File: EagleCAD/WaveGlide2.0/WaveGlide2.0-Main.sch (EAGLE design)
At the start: 58 parts, among them CN3 0, IC1 MC33502D, K2 MS-20-310-HN, Q2 reset, U1 ATMEGA328P_TQFP, U2 BMP180, U3 MPXV7002, U4 TPS55340PWP, U5 UG-2828GDEDF11, U6 TPS61222DCKR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

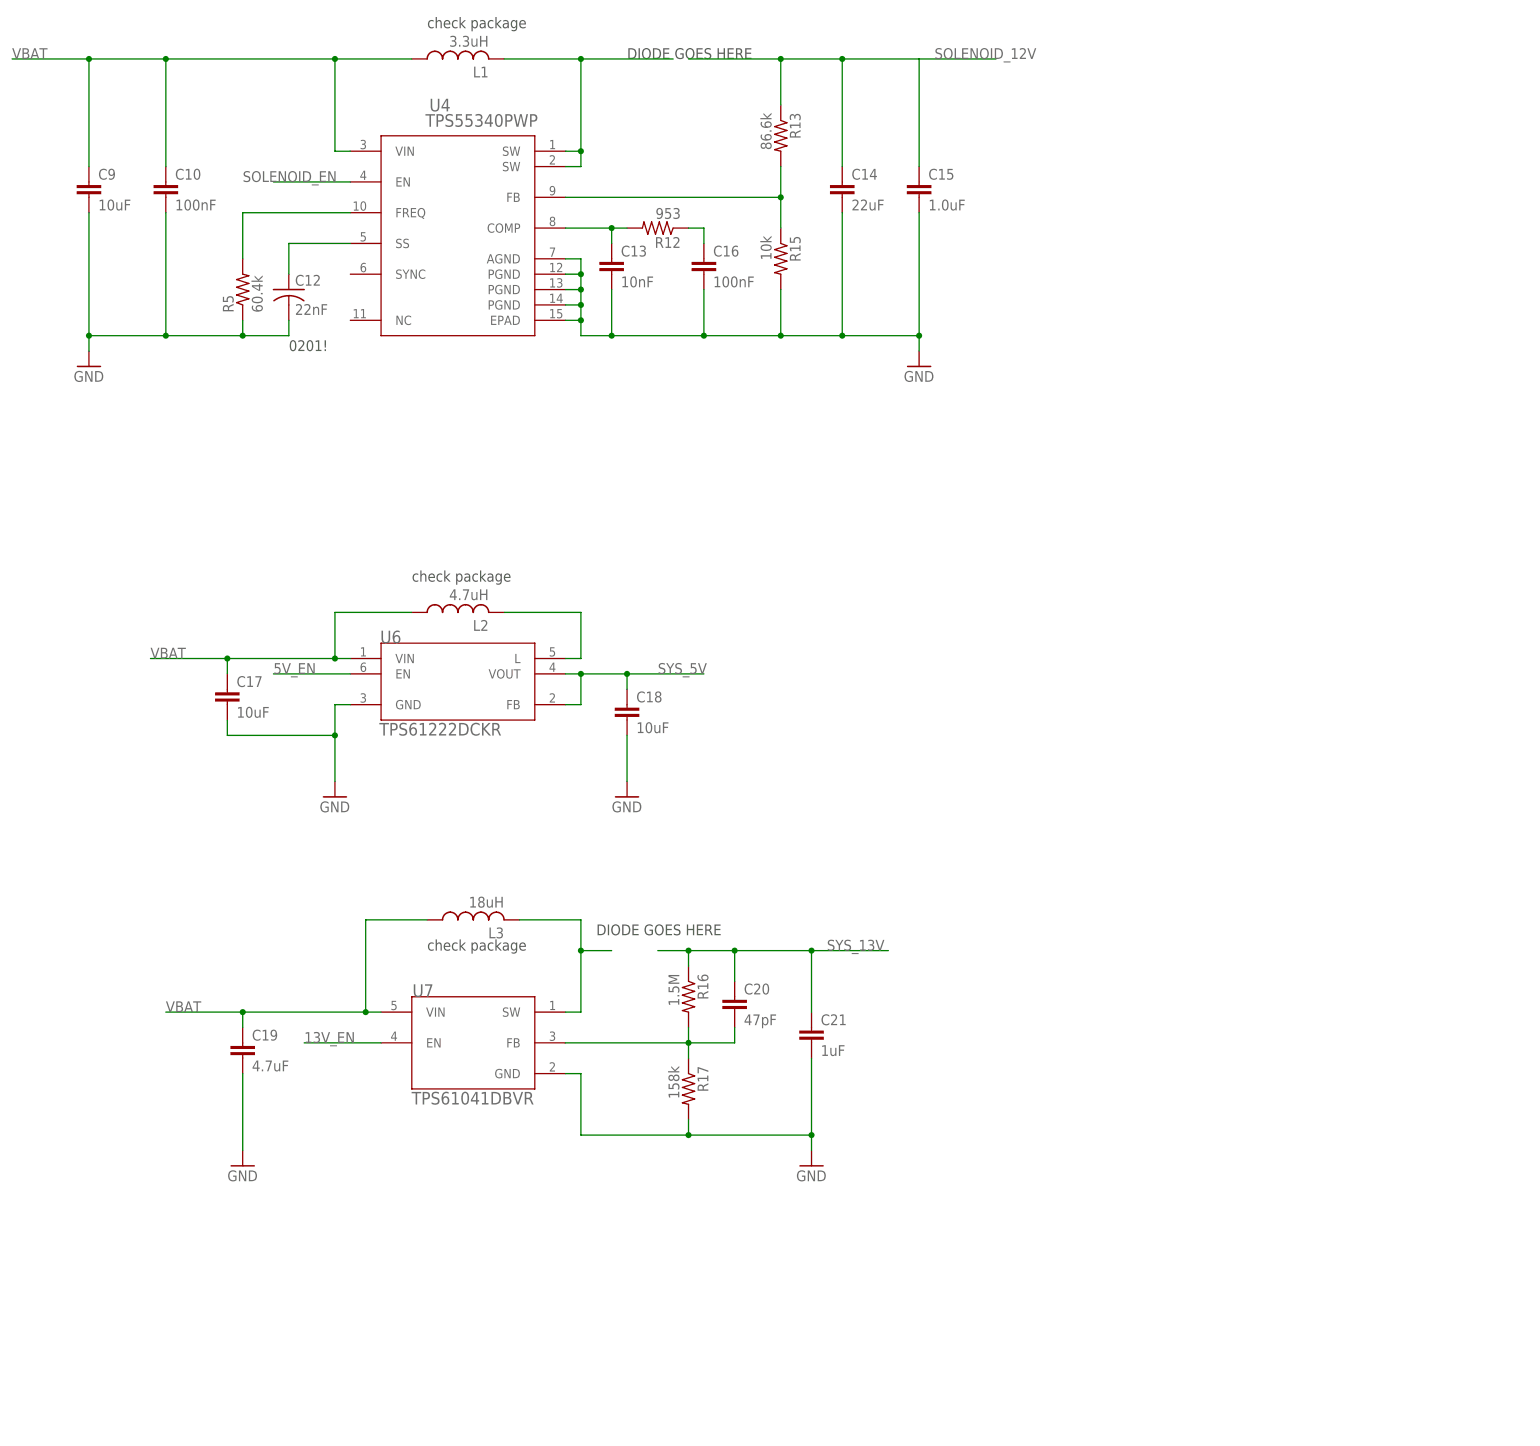
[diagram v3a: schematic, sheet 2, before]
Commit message: Add 3V3 Regulator
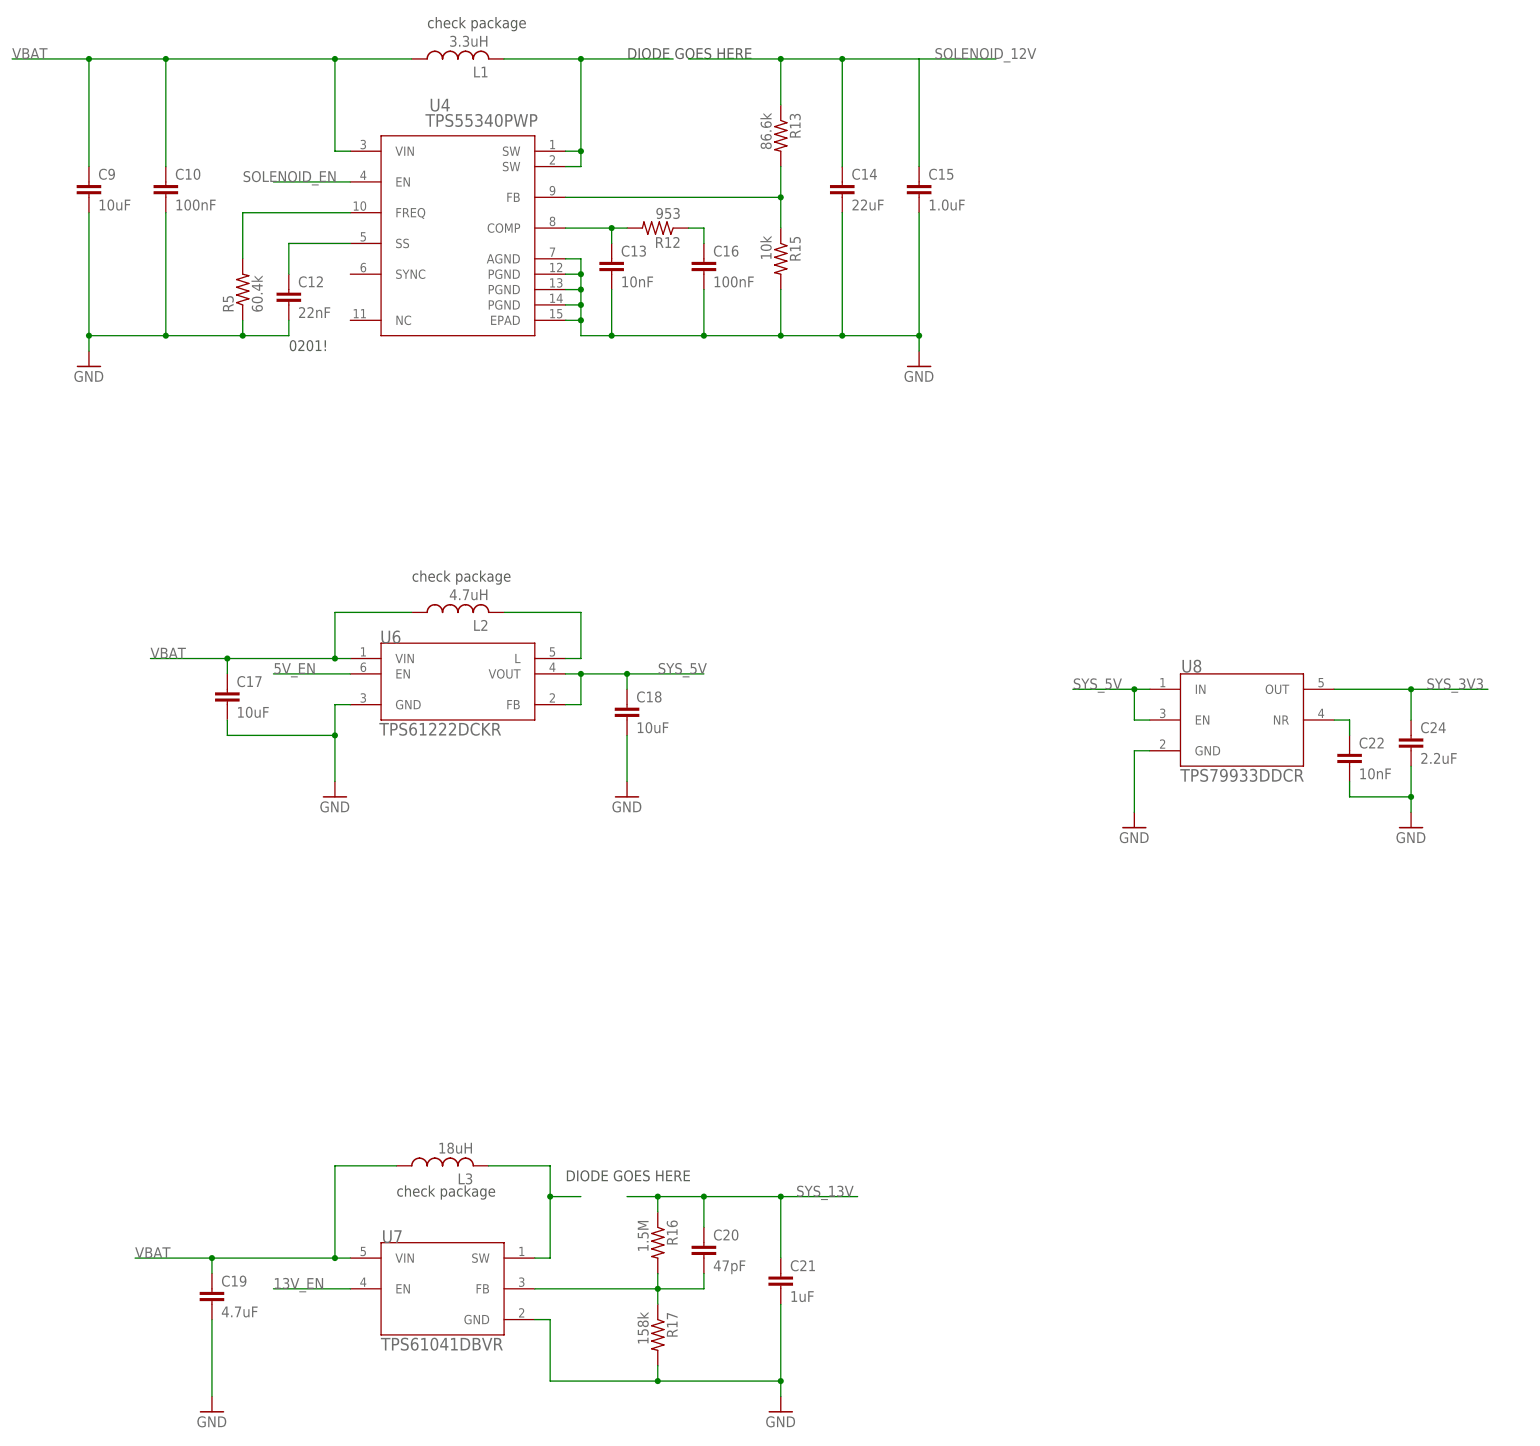
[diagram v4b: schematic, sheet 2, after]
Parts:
- added C22: 10nF, resistor:C-EUC0402
- added C24: 2.2uF, resistor:C-EUC0402
- added U8: TPS79933DDCR, CustomParts:TPS79933DDCR
- C12: device resistor:C-USC0201 -> resistor:C-EUC0402; MPN GRM033R60J223KE01D -> GRM155R60J223KA01D; TOL (none) -> 10%; VOLT (none) -> 6.3V
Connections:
- new net N$11: C22.1, U8.NR
- net GND: now also C22.2, C24.2, U8.GND
- net SYS_3V3: now also C24.1, U8.OUT
- net SYS_5V: now also U8.EN, U8.IN
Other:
- moved on the sheet: C19, C20, C21, L3, R16, R17, U7

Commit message: Add diodes to power regulators
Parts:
- added D4: SCHOTTKYDPAK, CustomParts:SCHOTTKYDPAK
- added D5: SCHOTTKYSOT-123, CustomParts:SCHOTTKYSOT-123
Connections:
- net N$11 renamed TPS79933_NR
- net N$6 renamed TPS61222_L
- net N$5: now also D5.A
- net SOLENOID_12V: now also D4.C
- net SYS_13V: now also D5.C
- net TPS55340_SW: now also D4.A
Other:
- note added: "Replace this symbol"
- note removed: "DIODE GOES HERE"
- moved on the sheet: C20, C21, C22, C24, R16, R17, U8
